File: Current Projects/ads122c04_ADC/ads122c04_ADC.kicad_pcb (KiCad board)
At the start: 2 copper layers, 50.8 x 27.9 mm, 38 parts, among them J1 Conn_01x05, J2 Conn_01x06, U1 ADS122C04IPWR, U2 MCP1711T-33I/OT

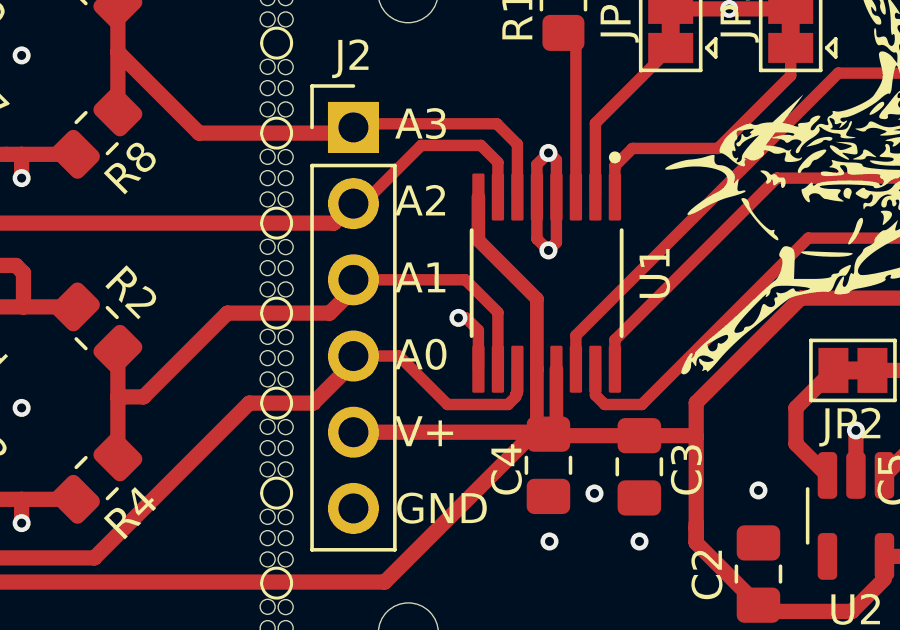
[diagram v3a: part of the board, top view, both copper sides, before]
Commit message: Added gerbers for ordering. Fixed issues with the reference voltage.
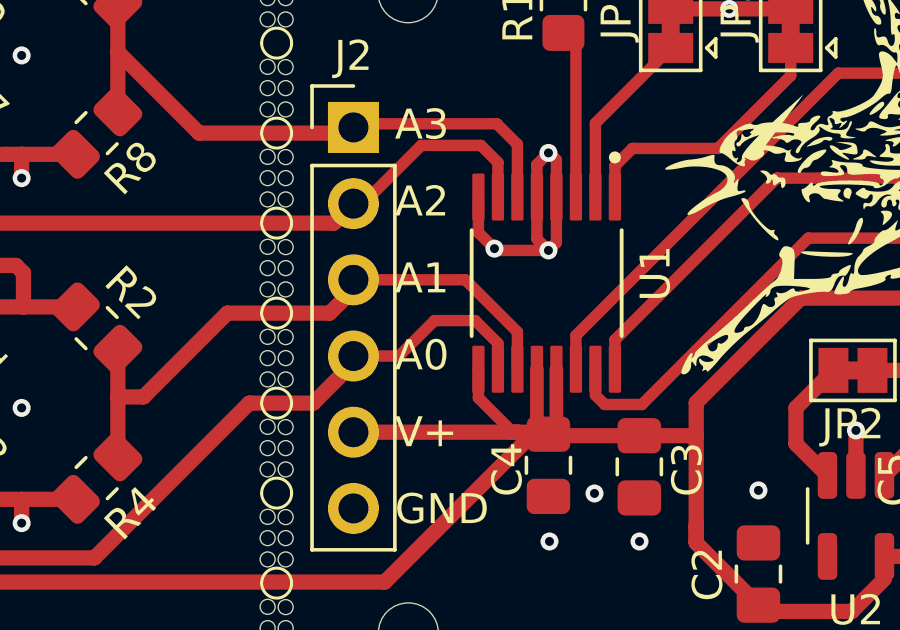
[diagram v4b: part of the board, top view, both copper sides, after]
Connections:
- U1 pad 10: /G0- -> /G0+
- U1 pad 11: /G0+ -> /G0-
- U1 pad 8: +3.3V -> GND
- U1 pad 9: GND -> +3.3V
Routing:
- net +3.3V: track 172.3 -> 168.5 mm
- net GND: track 23.9 -> 25.6 mm
- net /G0+: track 34.2 -> 33.5 mm
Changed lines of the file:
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@@
 		(allow_soldermask_bridges_in_footprints no)
 		(tenting front back)
-		(aux_axis_origin 99.06 105.41)
-		(grid_origin 99.06 105.41)
+		(aux_axis_origin 99.06 107.95)
+		(grid_origin 99.06 107.95)
 		(pcbplotparams
-			(layerselection 0x00000000_00000000_55555555_5755f5ff)
+			(layerselection 0x00000000_00000000_55555555_575755ff)
 			(plot_on_all_layers_selection 0x00000000_00000000_00000000_00000000)
 			(disableapertmacros no)
@@
 			(outputformat 1)
 			(mirror no)
-			(drillshape 1)
+			(drillshape 0)
 			(scaleselection 1)
 			(outputdirectory "")
@@
 			(layers "F.Cu" "F.Mask" "F.Paste")
 			(roundrect_rratio 0.125)
-			(net 1 "+3.3V")
+			(net 2 "GND")
 			(pinfunction "REFN")
 			(pintype "input")
@@
 			(layers "F.Cu" "F.Mask" "F.Paste")
 			(roundrect_rratio 0.125)
-			(net 2 "GND")
+			(net 1 "+3.3V")
 			(pinfunction "REFP")
 			(pintype "input")
@@
 			(layers "F.Cu" "F.Mask" "F.Paste")
 			(roundrect_rratio 0.125)
-			(net 8 "/G0-")
+			(net 9 "/G0+")
 			(pinfunction "AIN1")
 			(pintype "input")
@@
 			(layers "F.Cu" "F.Mask" "F.Paste")
 			(roundrect_rratio 0.125)
-			(net 9 "/G0+")
+			(net 8 "/G0-")
 			(pinfunction "AIN0")
 			(pintype "input")
@@
 	)
 	(segment
+		(start 121.725001 96.37)
+		(end 121.715 96.37)
+		(width 0.381)
+		(layer "F.Cu")
+		(net 1)
+	)
+	(segment
 		(start 128.985 101.51)
 		(end 128.985 102.16)
@@
 	)
 	(segment
-		(start 123.675 96.37)
-		(end 123.675 94.025)
-		(width 0.4572)
-		(layer "F.Cu")
-		(net 1)
-	)
-	(segment
 		(start 104.56 81.16)
 		(end 105.177107 81.16)
@@
 	)
 	(segment
+		(start 121.725001 97.324867)
+		(end 121.725001 96.37)
+		(width 0.381)
+		(layer "F.Cu")
+		(net 1)
+	)
+	(segment
 		(start 124.110787 98.585787)
 		(end 124.06 98.535)
@@
 	)
 	(segment
-		(start 143.06 85.66)
-		(end 141.9 84.5)
+		(start 123.06 98.47)
+		(end 122.870134 98.47)
 		(width 0.508)
 		(layer "F.Cu")
@@
 	)
 	(segment
-		(start 123.675 96.37)
-		(end 123.675 98.15)
-		(width 0.4572)
+		(start 143.06 85.66)
+		(end 141.9 84.5)
+		(width 0.508)
 		(layer "F.Cu")
 		(net 1)
 	)
 	(segment
-		(start 121.725001 92.075001)
-		(end 121.725001 90.63)
+		(start 123.675 96.37)
+		(end 123.675 98.15)
 		(width 0.4572)
 		(layer "F.Cu")
@@
 	)
 	(segment
+		(start 122.870134 98.47)
+		(end 121.725001 97.324867)
+		(width 0.381)
+		(layer "F.Cu")
+		(net 1)
+	)
+	(segment
 		(start 123.995 98.47)
 		(end 124.06 98.535)
@@
 	)
 	(segment
-		(start 123.675 94.025)
-		(end 121.725001 92.075001)
-		(width 0.4572)
-		(layer "F.Cu")
-		(net 1)
-	)
-	(segment
 		(start 124.56 83.16)
 		(end 128.035 83.16)
@@
 	)
 	(segment
-		(start 117.56 98.47)
+		(start 123.06 98.47)
 		(end 123.995 98.47)
 		(width 0.508)
@@
 	)
 	(segment
+		(start 117.56 98.47)
+		(end 123.06 98.47)
+		(width 0.508)
+		(layer "F.Cu")
+		(net 1)
+	)
+	(segment
 		(start 124.325 96.37)
 		(end 124.325 98.27)
@@
 	)
 	(segment
+		(start 122.32 92.41)
+		(end 121.725001 91.815001)
+		(width 0.381)
+		(layer "F.Cu")
+		(net 2)
+	)
+	(segment
 		(start 124.088374 89.16)
 		(end 124.325 89.396626)
@@
 	)
 	(segment
-		(start 121.725001 95.075001)
-		(end 121.725001 96.37)
+		(start 124.06 92.41)
+		(end 122.32 92.41)
 		(width 0.381)
 		(layer "F.Cu")
@@
 	)
 	(segment
-		(start 121.06 94.66)
-		(end 121.31 94.66)
-		(width 0.381)
-		(layer "F.Cu")
-		(net 2)
-	)
-	(segment
 		(start 124.325 92.145)
 		(end 124.06 92.41)
@@
 	)
 	(segment
-		(start 121.31 94.66)
-		(end 121.725001 95.075001)
-		(width 0.381)
-		(layer "F.Cu")
-		(net 2)
-	)
-	(segment
 		(start 108.292893 89.207107)
 		(end 106.5 89.207107)
@@
 	)
 	(segment
+		(start 121.725001 91.815001)
+		(end 121.725001 90.63)
+		(width 0.381)
+		(layer "F.Cu")
+		(net 2)
+	)
+	(segment
 		(start 106.5 89.207107)
 		(end 106 89.207107)
@@
 	)
 	(via
+		(at 122.26 92.35)
+		(size 0.6)
+		(drill 0.3)
+		(layers "F.Cu" "B.Cu")
+		(net 2)
+	)
+	(via
 		(at 124.06 89.16)
 		(size 0.6)
@@
 	)
 	(via
-		(at 121.06 94.66)
-		(size 0.6)
-		(drill 0.3)
-		(layers "F.Cu" "B.Cu")
-		(net 2)
-	)
-	(via
 		(at 106.5 85.91)
 		(size 0.6)
@@
 	)
 	(segment
-		(start 122.375 96.37)
-		(end 122.375 94.475)
-		(width 0.381)
+		(start 109.707107 97.292893)
+		(end 109.707107 99.292893)
+		(width 0.508)
 		(layer "F.Cu")
 		(net 8)
 	)
 	(segment
-		(start 109.707107 97.292893)
-		(end 109.707107 99.292893)
-		(width 0.508)
+		(start 118.120001 93.39)
+		(end 118 93.269999)
+		(width 0.381)
 		(layer "F.Cu")
 		(net 8)
 	)
 	(segment
-		(start 122.375 94.475)
-		(end 121.29 93.39)
+		(start 121.29 93.39)
+		(end 123.024999 95.124999)
 		(width 0.381)
 		(layer "F.Cu")
@@
 	)
 	(segment
-		(start 118.120001 93.39)
-		(end 118 93.269999)
+		(start 123.024999 95.124999)
+		(end 123.024999 96.37)
 		(width 0.381)
 		(layer "F.Cu")
@@
 	)
 	(segment
-		(start 122.9715 97.208498)
-		(end 122.9715 97.288564)
+		(start 120.26 94.75)
+		(end 121.620065 94.75)
+		(width 0.381)
+		(layer "F.Cu")
+		(net 9)
+	)
+	(segment
+		(start 121.620065 94.75)
+		(end 122.375 95.504935)
+		(width 0.381)
+		(layer "F.Cu")
+		(net 9)
+	)
+	(segment
+		(start 118 95.81)
+		(end 118.12 95.93)
+		(width 0.381)
+		(layer "F.Cu")
+		(net 9)
+	)
+	(segment
+		(start 118.12 95.93)
+		(end 119.08 95.93)
 		(width 0.381)
 		(layer "F.Cu")
@@
 	)
 	(segment
-		(start 123.024999 96.37)
-		(end 123.024999 97.154999)
-		(width 0.381)
-		(layer "F.Cu")
-		(net 9)
-	)
-	(segment
-		(start 122.9715 97.288564)
-		(end 122.713564 97.5465)
+		(start 122.375 95.504935)
+		(end 122.375 96.37)
 		(width 0.381)
 		(layer "F.Cu")
@@
 	)
 	(segment
-		(start 122.713564 97.5465)
-		(end 120.6965 97.5465)
-		(width 0.381)
-		(layer "F.Cu")
-		(net 9)
-	)
-	(segment
 		(start 104.16 102.66)
 		(end 101.292893 99.792893)
@@
 	)
 	(segment
-		(start 123.024999 97.154999)
-		(end 122.9715 97.208498)
-		(width 0.381)
-		(layer "F.Cu")
-		(net 9)
-	)
-	(segment
-		(start 120.6965 97.5465)
-		(end 119.08 95.93)
+		(start 119.08 95.93)
+		(end 120.26 94.75)
 		(width 0.381)
 		(layer "F.Cu")
@@
 		(layer "F.Cu")
 		(net 9)
-	)
-	(segment
-		(start 119.08 95.93)
-		(end 118.12 95.93)
-		(width 0.381)
-		(layer "F.Cu")
-		(net 9)
-	)
-	(segment
-		(start 118.12 95.93)
-		(end 118 95.81)
-		(width 0.381)
-		(layer "F.Cu")
-		(net 9)

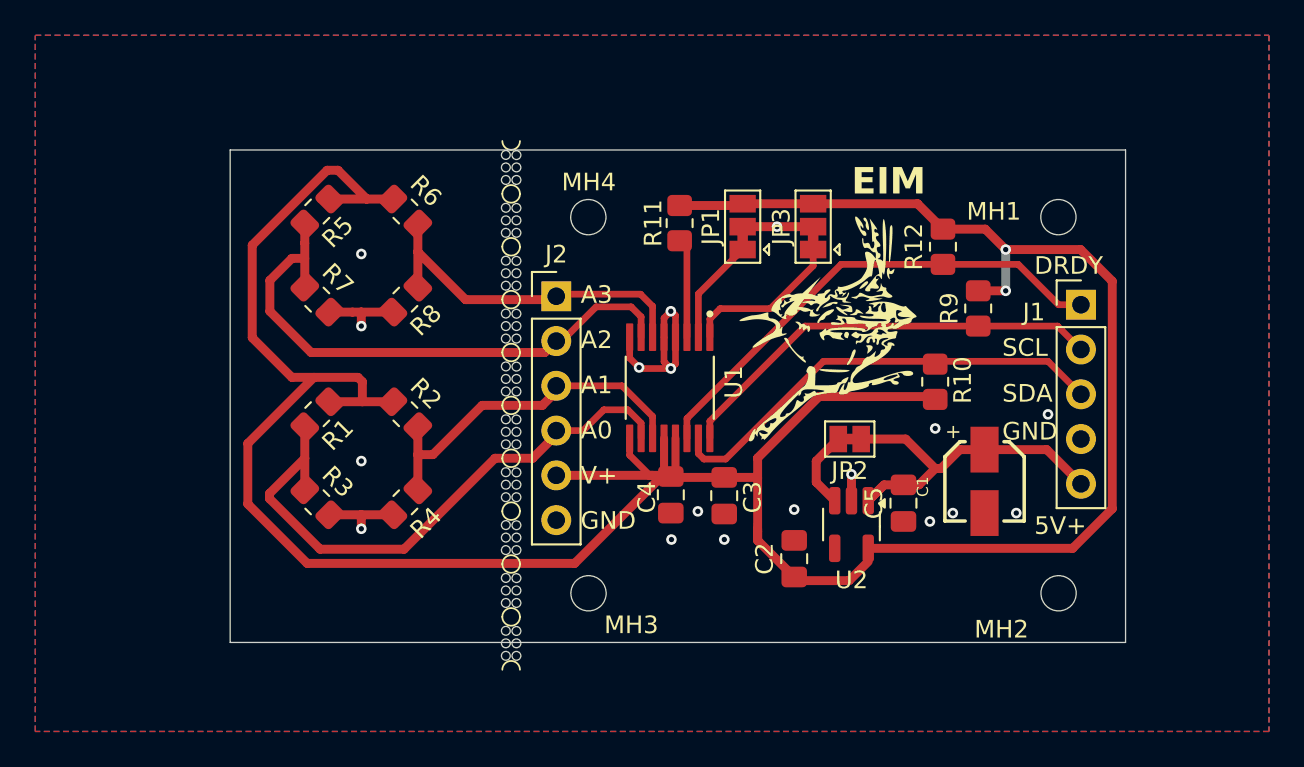
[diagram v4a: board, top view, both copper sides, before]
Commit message: Added wolf silkscreen to back of board.
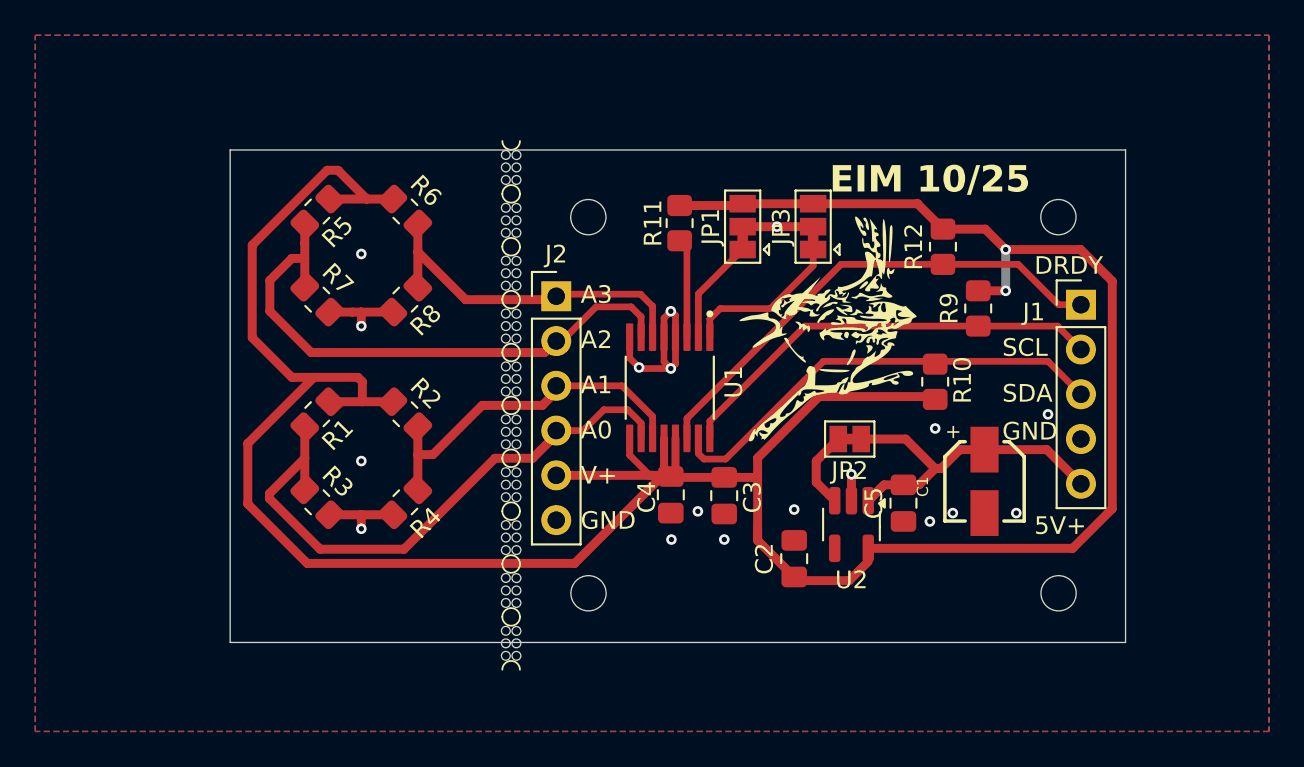
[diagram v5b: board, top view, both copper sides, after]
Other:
- board text added: "EIM 10/25"
- board text removed: "EIM"
